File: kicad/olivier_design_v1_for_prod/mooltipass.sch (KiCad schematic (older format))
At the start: 66 parts, among them CON2 CON_10118194-0001LF, P1 CONN_8, P2 CONN_6, P3 CONN_10, P4 CONN_8, P5 CONN_1, P6 CONN_1, P7 CONN_1, P8 CONN_1, Q1 MOS_P, Q2 MOS_N, Q3 MOS_P, Q4 MOS_N, U1 CON_SFV30R-2STE1HLF, U2 CON_7312P0225A13LF, U3 IP4234CZ6,125, U4 ATMEGA32U4_QFN, U5 ST662ACD, U6 AT45DB011D-SSH, U7 CON_STACK_9, X1 16MHz

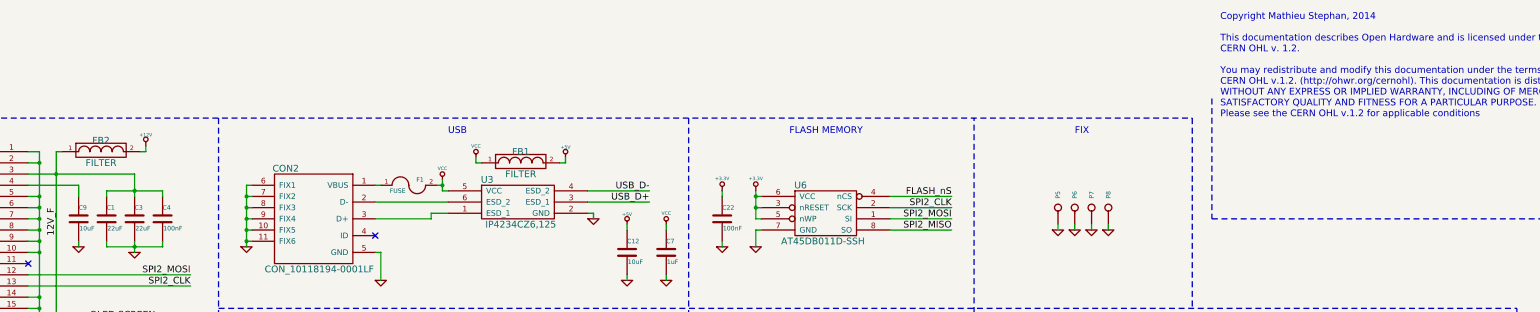
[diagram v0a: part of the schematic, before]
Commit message: solved noisy power supply and voltage ripple
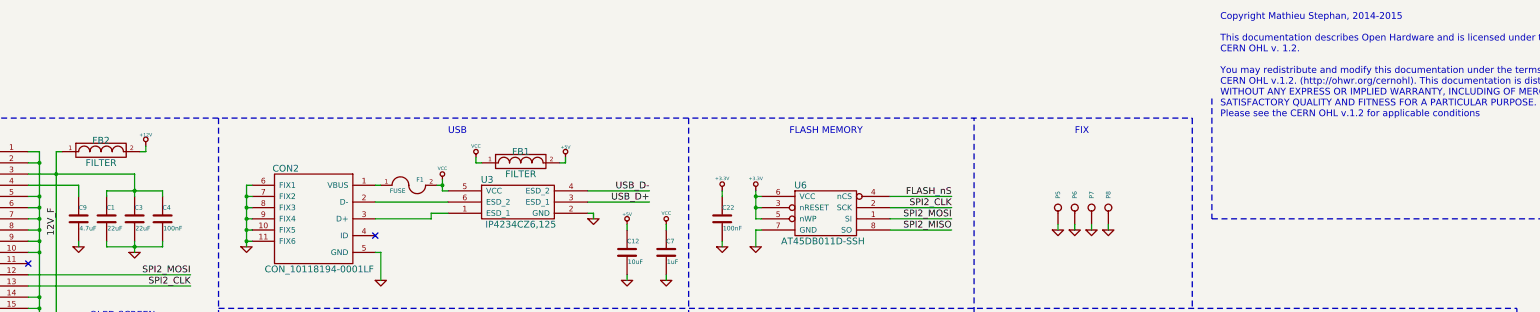
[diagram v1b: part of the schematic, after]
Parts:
- C9: value 10uF -> 4.7uF
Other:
- note added: "Copyright Mathieu Stephan, 2014-2015\n\nThis documentation describes Open Hardware and is licensed under the\nCERN OHL v. 1.2.\n\nYou may redistribute and modify this documentation under the terms of the\nCERN OHL v.1.2. (http://ohwr.org/cernohl). This documentation is distributed\nWITHOUT ANY EXPRESS OR IMPLIED WARRANTY, INCLUDING OF MERCHANTABILITY,\nSATISFACTORY QUALITY AND FITNESS FOR A PARTI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"
- note removed: "Copyright Mathieu Stephan, 2014\n\nThis documentation describes Open Hardware and is licensed under the\nCERN OHL v. 1.2.\n\nYou may redistribute and modify this documentation under the terms of the\nCERN OHL v.1.2. (http://ohwr.org/cernohl). This documentation is distributed\nWITHOUT ANY EXPRESS OR IMPLIED WARRANTY, INCLUDING OF MERCHANTABILITY,\nSATISFACTORY QUALITY AND FITNESS FOR A PARTICULAR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"
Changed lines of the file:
@@
 Sheet 1 1
 Title "M. Stephan - Mooltipass Schematics (Licensed under CERN OHL V1.2)"
-Date "28 feb 2015"
+Date "17 apr 2015"
 Rev "2"
 Comp ""
@@
 P 2200 1550
 F 0 "C9" H 2200 1650 40  0000 L CNN
-F 1 "10uF" H 2206 1465 40  0000 L CNN
+F 1 "4.7uF" H 2206 1465 40  0000 L CNN
 F 2 "~" H 2238 1400 30  0000 C CNN
 F 3 "~" H 2200 1550 60  0000 C CNN
@@
 $EndComp
 Text Notes 12400 650  0    60   ~ 0
-Copyright Mathieu Stephan, 2014\n\nThis documentation describes Open Hardware and is licensed under the\nCERN OHL v. 1.2.\n\nYou may redistribute and modify this documentation under the terms of the\nCERN OHL v.1.2. (http://ohwr.org/cernohl). This documentation is distributed\nWITHOUT ANY EXPRESS OR IMPLIED WARRANTY, INCLUDING OF MERCHANTABILITY,\nSATISFACTORY QUALITY AND FITNESS FOR A PARTICULAR PURPOSE. \nPlease see the CERN OHL v.1.2 for applicable conditions
+Copyright Mathieu Stephan, 2014-2015\n\nThis documentation describes Open Hardware and is licensed under the\nCERN OHL v. 1.2.\n\nYou may redistribute and modify this documentation under the terms of the\nCERN OHL v.1.2. (http://ohwr.org/cernohl). This documentation is distributed\nWITHOUT ANY EXPRESS OR IMPLIED WARRANTY, INCLUDING OF MERCHANTABILITY,\nSATISFACTORY QUALITY AND FITNESS FOR A PARTICULAR PURPOSE. \nPlease see the CERN OHL v.1.2 for applicable conditions
 $Comp
 L C C3
